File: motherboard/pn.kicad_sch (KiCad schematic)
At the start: 80 parts, among them J201 BNC, J202 Conn_01x05, J203 BNC, Q201 2N7002, Q202 2N7002, Q203 2N7002, U201 LMH6609, U202 SYPD-1, U203 LM393, U204 AD797AR, U205 LM393, U206 OPA192IDR

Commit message: use SOIC-8 for OPA192IDR
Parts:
- U206: footprint Package_SO:VSSOP-8_3x3mm_P0.65mm -> Package_SO:SOIC-8_3.9x4.9mm_P1.27mm; MPN OPA192ID -> OPA192IDR

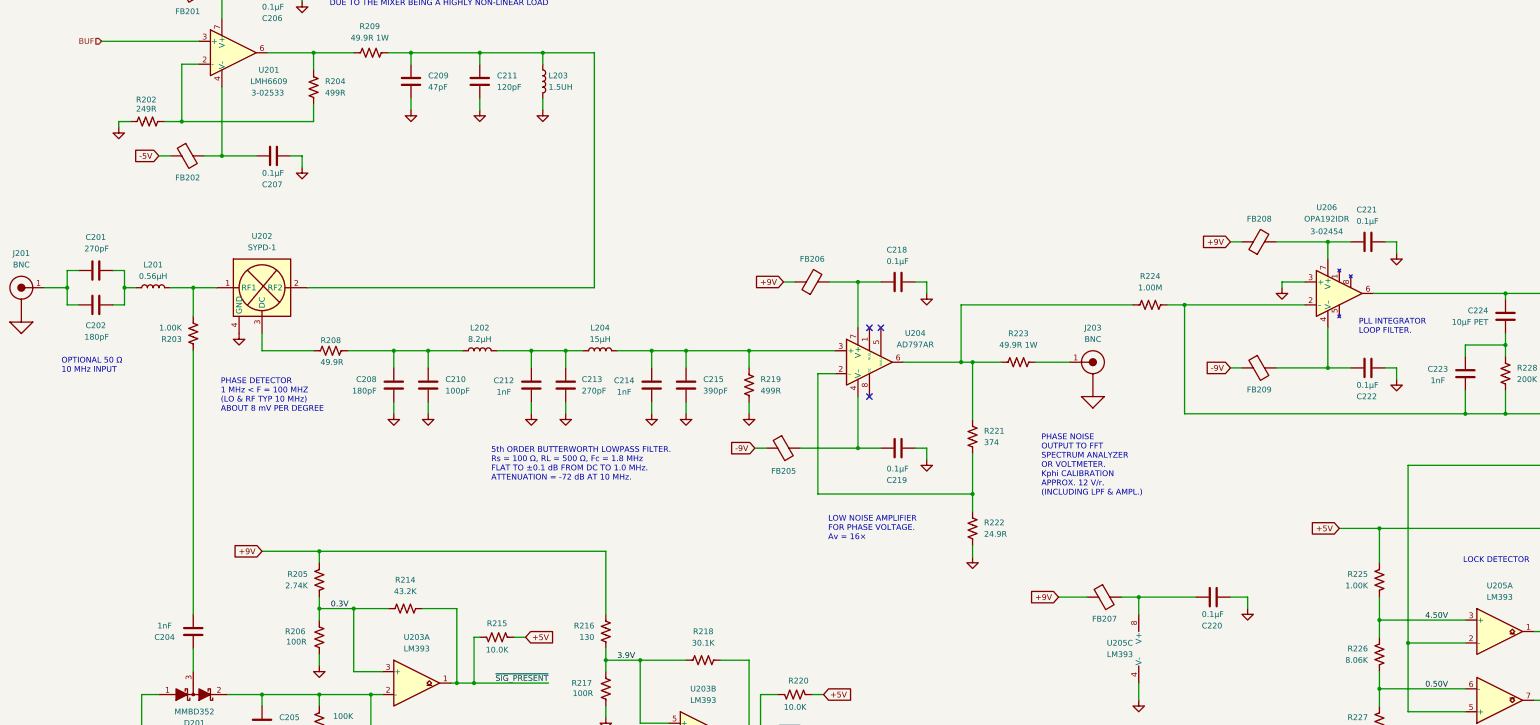
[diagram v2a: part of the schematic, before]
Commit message: add ESD protection (14V TVS)
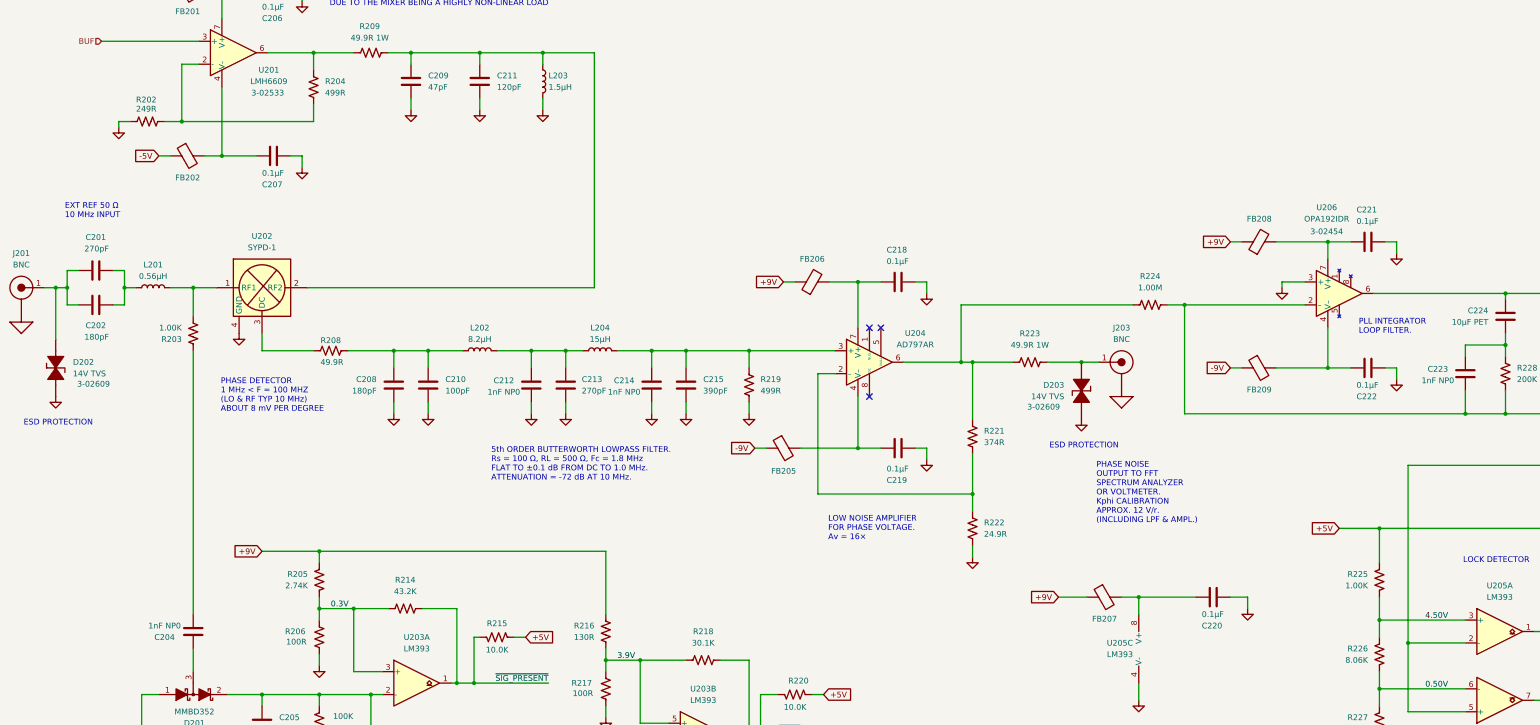
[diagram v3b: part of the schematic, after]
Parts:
- added D202, D203: 14V TVS, Capacitor_SMD:C_0402_1005Metric, symbol #SRS:3_ICs/3-02609
- C204, C212, C214, C223: value 1nF -> 1nF NP0
- L203: value 1.5UH -> 1.5μH
- R216: value 130 -> 130R
- R221: value 374 -> 374R
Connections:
- net GND: now also D202.2 (ANODE), D203.2 (ANODE)
- net at J203.1 (C), R223.2: now also D203.1 (CATHODE)
- net at C201.1, C202.1, J201.1 (C): now also D202.1 (CATHODE)
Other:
- note added: "ESD PROTECTION"
- note added: "EXT REF 50 Ω 10 MHz INPUT"
- note removed: "OPTIONAL 50 Ω 10 MHz INPUT"
- moved on the sheet: J203, R223

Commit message: add schematic annotations
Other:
- note added: "MATES TO LED BOARD 7-01993 WITH GREEN/GREEN/GREEN/RED LEDS INSTALLED, VIA SHORT 5 POS RIBBON CABLE (1-01043)"

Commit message: retune comparator thresholds for 1--3 Vpp
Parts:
- removed R216: 130R, Resistor_SMD:R_0603_1608Metric, symbol #SRS:4_Resistors/4-02072
- removed R217: 100R, Resistor_SMD:R_0603_1608Metric, symbol #SRS:4_Resistors/4-02061
- added R217: 10.0K, Resistor_SMD:R_0603_1608Metric, symbol #SRS:4_Resistors/4-02253
- added R218: 1.00M, Resistor_SMD:R_0603_1608Metric, symbol #SRS:4_Resistors/4-02445
- renumbered R218 to R216
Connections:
- net +9V: now also R216.2
- net GND: now also R217.1
- net ~{OVLD}: now also R218.2; no longer R216.2
- net 3.9V renamed 2.3V
- net 2.3V: now also R217.2, R218.1
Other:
- note added: "TRIPS @ 0.9 VPP"
- note added: "TRIPS @ 3.3 VPP CLEARS @ 2.8 VPP"
- moved on the sheet: R216

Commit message: update OCXO bead to SMB2.5R-2 (higher current)
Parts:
- D202, D203: Footprint Modified By assignment_engine -> (none); Footprint Modified Timestamp 2025-10-13 21:00:11 -0800 -> (none); Imported from Altium 2025-07-21 -> (none); JLCPCB (none) -> C7473167; Manf Littelfuse Inc. -> (none); Price 0.15 -> (none); Qty In Stock 9228 -> (none); Recommended Y -> (none); Symbol DISC_SRS:DIODE-TVS -> (none); Symbol Modified By assignment_engine -> (none); Symbol Modified Timestamp 2025-10-13 21:00:11 -0800 -> (none); Tempco (none) -> (none); Used In FS740,FS752 -> (none)

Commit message: add testpoints
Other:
- note added: "PHASE DETECTOR 1 MHz < F = 100 MHz (LO & RF TYP 10 MHz) ABOUT 8 mV PER DEGREE"
- note added: "TRIPS @ 0.9 Vpp"
- note added: "TRIPS @ 3.3 Vpp CLEARS @ 2.8 Vpp"
- note removed: "PHASE DETECTOR 1 MHz < F = 100 MHZ (LO & RF TYP 10 MHz) ABOUT 8 mV PER DEGREE"
- note removed: "TRIPS @ 0.9 VPP"
- note removed: "TRIPS @ 3.3 VPP CLEARS @ 2.8 VPP"

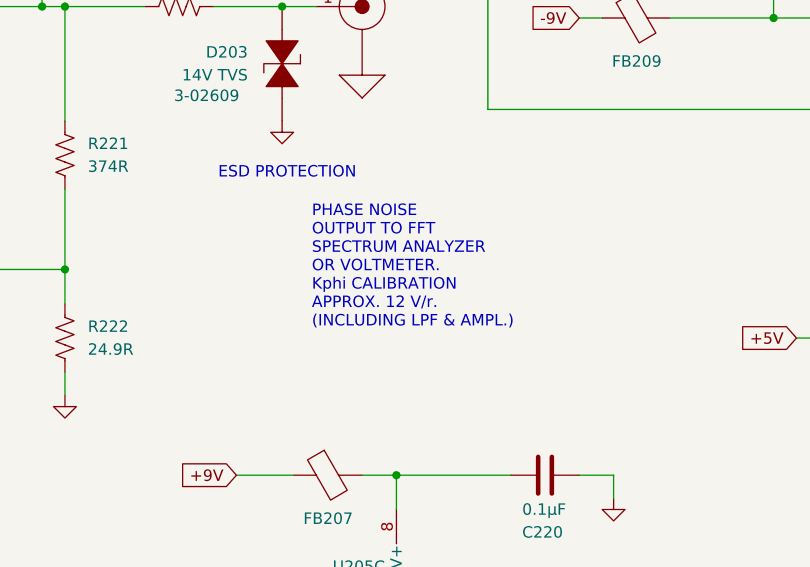
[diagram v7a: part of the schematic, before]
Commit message: fix annotations
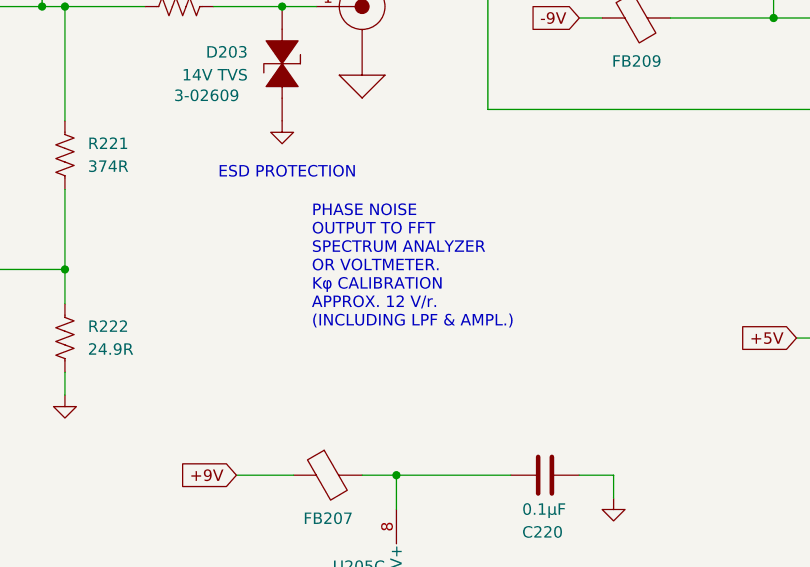
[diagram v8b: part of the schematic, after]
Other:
- note added: "PHASE NOISE OUTPUT TO FFT SPECTRUM ANALYZER OR VOLTMETER. Kφ CALIBRATION APPROX. 12 V/r. (INCLUDING LPF & AMPL.)"
- note removed: "PHASE NOISE OUTPUT TO FFT SPECTRUM ANALYZER OR VOLTMETER. Kphi CALIBRATION APPROX. 12 V/r. (INCLUDING LPF & AMPL.)"
